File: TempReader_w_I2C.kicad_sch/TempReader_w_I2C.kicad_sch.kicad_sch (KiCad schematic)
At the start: 33 parts, among them J1 NRF Pin Header, J2 BME Pin Header, J3 NOT SURE WHAT THIS IS, J4 Also this, U1 STM32F030K6Tx, U2 nRF24L01P, U4 BME280, U5 MIC5205-3.3YM5, Y1 16MH

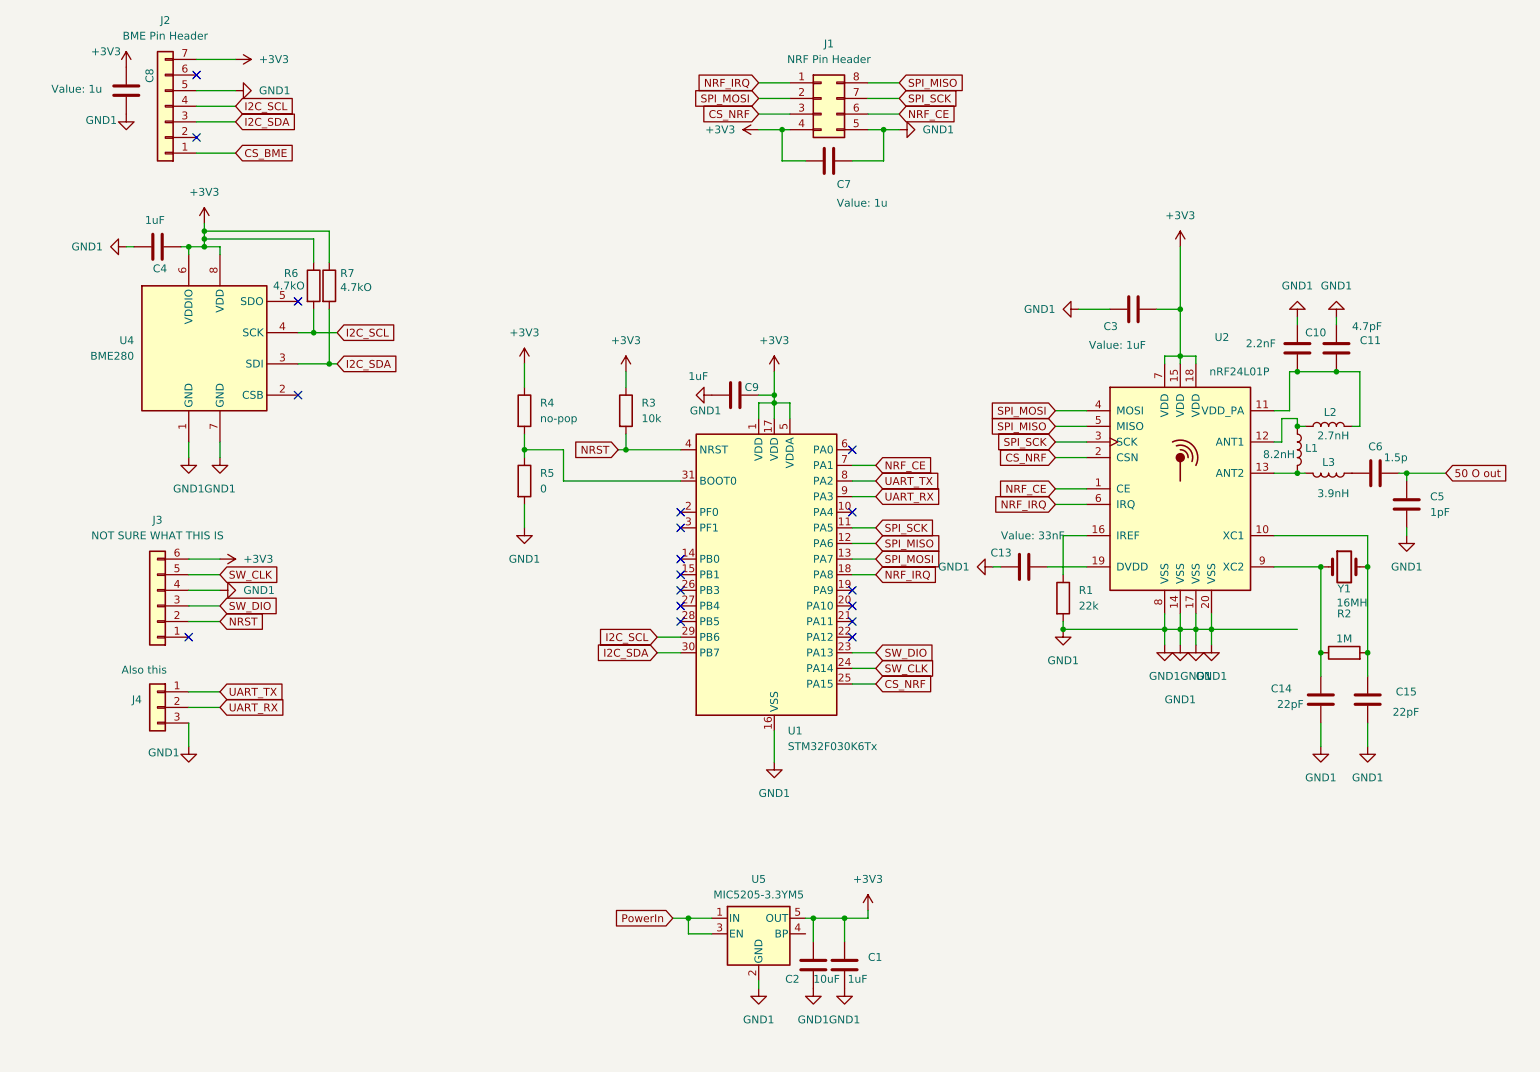
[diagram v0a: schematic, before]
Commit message: Update TempReader_w_I2C.kicad_sch/TempReader_w_I2C.kicad_sch.kicad_pcb
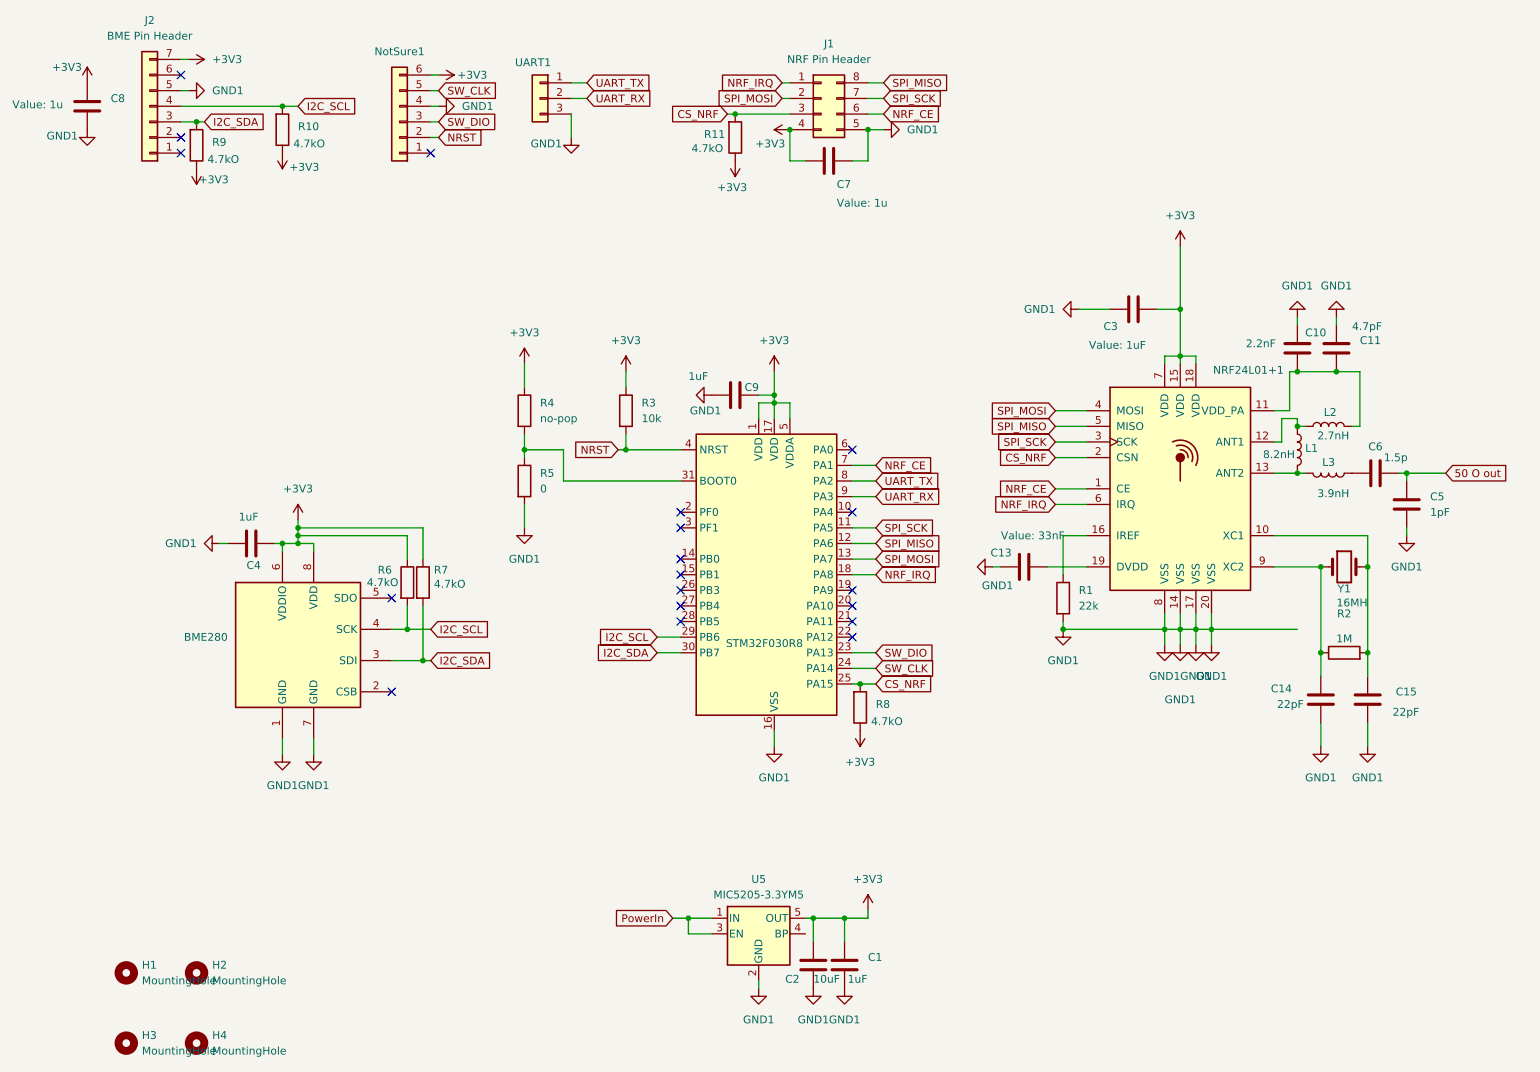
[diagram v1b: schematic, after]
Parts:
- added H1, H2, H3, H4: MountingHole, MountingHole:MountingHole_2.2mm_M2, symbol Mechanical:MountingHole
- added R10, R11, R8, R9: 4.7kO, Resistor_SMD:R_0603_1608Metric_Pad0.98x0.95mm_HandSolder, symbol Device:R
- NRF24L01+1: renamed from U2; value nRF24L01P -> ~
- STM32F030R8: renamed from U1; value STM32F030K6Tx -> ~
- UART1: renamed from J4; value Also this -> UART
- renumbered U4 to BME280, J3 to NotSure1
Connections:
- net +3V3: now also R10.1, R11.1, R8.1, R9.1
- net CS_NRF: now also R11.2, R8.2
- net I2C_SCL: now also R10.2
- net I2C_SDA: now also R9.2
- net CS_BME: no longer names the net of J2.1 (Pin_1)
- no-connect marks 18 -> 19
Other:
- moved on the sheet: BME280, C4, J2, NotSure1, R6, R7, UART1

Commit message: Set payload length
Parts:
- renumbered C6 to C5, C5 to C6
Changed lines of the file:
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@@
 		(dnp no)
 		(fields_autoplaced yes)
-		(property "Reference" "C5"
+		(property "Reference" "C6"
 			(at 245.11 91.4399 0)
 			(effects
@@
 			(project ""
 				(path "/dfa4cd9b-69e6-4963-8ce6-48aa9a425e97"
-					(reference "C5")
+					(reference "C6")
 					(unit 1)
 				)
@@
 		(on_board yes)
 		(dnp no)
-		(property "Reference" "C6"
+		(property "Reference" "C5"
 			(at 236.22 83.312 90)
 			(effects
@@
 			(project ""
 				(path "/dfa4cd9b-69e6-4963-8ce6-48aa9a425e97"
-					(reference "C6")
+					(reference "C5")
 					(unit 1)
 				)
